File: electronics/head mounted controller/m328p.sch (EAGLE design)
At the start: 40 parts, among them J2 M02PTH, U1 ATMEGA328P, U2 V_REG_MIC2920, X1 16MHz

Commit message: pre-production PCBs
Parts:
- removed U$1, U$2: JST-PH3, jst-ph:JST-PH3
- added HEAD-DATA, HEAD-PWR: (no value), jst-ph:JST-PH2
- LIM-X, LIM-Y, LIM-Z: value JST-PH3 -> (none); device jst-ph:JST-PH3 -> jst-ph:JST-PH2
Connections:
- net 12V: now also HEAD-PWR.1; no longer U$1.1
- net GND: now also HEAD-PWR.2; no longer U$1.2
- net RX: now also HEAD-DATA.1; no longer U$2.1
- net TX: now also HEAD-DATA.2; no longer U$2.2
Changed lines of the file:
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@@
 <part name="STANDOFF3" library="SparkFun-Electromechanical" deviceset="STAND-OFF" device="TIGHT"/>
 <part name="STANDOFF4" library="SparkFun-Electromechanical" deviceset="STAND-OFF" device="TIGHT"/>
-<part name="LIM-X" library="jst-ph" deviceset="JST-PH3" device=""/>
-<part name="LIM-Y" library="jst-ph" deviceset="JST-PH3" device=""/>
-<part name="LIM-Z" library="jst-ph" deviceset="JST-PH3" device=""/>
+<part name="LIM-X" library="jst-ph" deviceset="JST-PH2" device=""/>
+<part name="LIM-Y" library="jst-ph" deviceset="JST-PH2" device=""/>
+<part name="LIM-Z" library="jst-ph" deviceset="JST-PH2" device=""/>
 <part name="DRV-Z" library="SparkFun-Connectors" deviceset="M06" device="LOCK"/>
 <part name="DRV-Y" library="SparkFun-Connectors" deviceset="M06" device="LOCK"/>
@@
 <part name="AUX-X" library="SparkFun-Connectors" deviceset="M06" device="LOCK"/>
 <part name="GND3" library="SparkFun-Aesthetics" deviceset="GND" device=""/>
-<part name="U2" library="SparkFun-PowerIC" deviceset="V_REG_MIC2920" device=""/>
 <part name="GND4" library="SparkFun-Aesthetics" deviceset="GND" device=""/>
 <part name="C12" library="adafruit" deviceset="C-US" device="C1206" value="10u"/>
@@
 <part name="C3" library="adafruit" deviceset="C-US" device="C0603" value="100n"/>
 <part name="GND5" library="SparkFun-Aesthetics" deviceset="GND" device=""/>
-<part name="U$1" library="jst-ph" deviceset="JST-PH3" device=""/>
-<part name="U$2" library="jst-ph" deviceset="JST-PH3" device=""/>
+<part name="HEAD-PWR" library="jst-ph" deviceset="JST-PH2" device=""/>
+<part name="HEAD-DATA" library="jst-ph" deviceset="JST-PH2" device=""/>
 <part name="C9" library="adafruit" deviceset="C-US" device="C1206" value="10u"/>
 <part name="C10" library="adafruit" deviceset="C-US" device="C1206" value="10u"/>
 <part name="C11" library="adafruit" deviceset="C-US" device="C1206" value="10u"/>
+<part name="U2" library="SparkFun-PowerIC" deviceset="V_REG_MIC2920" device=""/>
 </parts>
 <sheets>
@@
 <instance part="AUX-X" gate="G$1" x="195.58" y="7.62"/>
 <instance part="GND3" gate="1" x="180.34" y="25.4"/>
-<instance part="U2" gate="G$1" x="154.94" y="104.14" smashed="yes">
-<attribute name="NAME" x="157.48" y="96.52" size="1.778" layer="95"/>
-</instance>
 <instance part="GND4" gate="1" x="154.94" y="91.44"/>
 <instance part="C12" gate="G$1" x="167.64" y="101.6"/>
@@
 <instance part="C3" gate="G$1" x="20.32" y="63.5"/>
 <instance part="GND5" gate="1" x="81.28" y="86.36"/>
-<instance part="U$1" gate="G$1" x="86.36" y="96.52" smashed="yes">
-<attribute name="NAME" x="83.82" y="102.362" size="1.778" layer="95"/>
-</instance>
-<instance part="U$2" gate="G$1" x="86.36" y="111.76" smashed="yes">
-<attribute name="NAME" x="83.82" y="117.602" size="1.778" layer="95"/>
+<instance part="HEAD-PWR" gate="G$1" x="86.36" y="96.52" smashed="yes">
+<attribute name="NAME" x="83.82" y="99.822" size="1.778" layer="95"/>
+</instance>
+<instance part="HEAD-DATA" gate="G$1" x="86.36" y="111.76" smashed="yes">
+<attribute name="NAME" x="83.82" y="115.062" size="1.778" layer="95"/>
 </instance>
 <instance part="C9" gate="G$1" x="124.46" y="101.6"/>
 <instance part="C10" gate="G$1" x="132.08" y="101.6"/>
 <instance part="C11" gate="G$1" x="139.7" y="101.6"/>
+<instance part="U2" gate="G$1" x="154.94" y="104.14" smashed="yes">
+<attribute name="NAME" x="157.48" y="96.52" size="1.778" layer="95"/>
+</instance>
 </instances>
 <busses>
@@
 <wire x1="60.96" y1="96.52" x2="81.28" y2="96.52" width="0.1524" layer="91"/>
 <wire x1="81.28" y1="96.52" x2="81.28" y2="88.9" width="0.1524" layer="91"/>
-<wire x1="93.98" y1="96.52" x2="99.06" y2="96.52" width="0.1524" layer="91"/>
+<wire x1="93.98" y1="93.98" x2="99.06" y2="93.98" width="0.1524" layer="91"/>
 <wire x1="81.28" y1="88.9" x2="99.06" y2="88.9" width="0.1524" layer="91"/>
-<wire x1="99.06" y1="88.9" x2="99.06" y2="96.52" width="0.1524" layer="91"/>
+<wire x1="99.06" y1="88.9" x2="99.06" y2="93.98" width="0.1524" layer="91"/>
 <junction x="81.28" y="88.9"/>
-<pinref part="U$1" gate="G$1" pin="2"/>
+<pinref part="HEAD-PWR" gate="G$1" pin="2"/>
 </segment>
 <segment>
@@
 <wire x1="170.18" y1="58.42" x2="175.26" y2="58.42" width="0.1524" layer="91"/>
 <wire x1="175.26" y1="58.42" x2="195.58" y2="58.42" width="0.1524" layer="91"/>
-<wire x1="193.04" y1="66.04" x2="195.58" y2="66.04" width="0.1524" layer="91"/>
-<wire x1="195.58" y1="66.04" x2="195.58" y2="58.42" width="0.1524" layer="91"/>
+<wire x1="193.04" y1="63.5" x2="195.58" y2="63.5" width="0.1524" layer="91"/>
+<wire x1="195.58" y1="63.5" x2="195.58" y2="58.42" width="0.1524" layer="91"/>
 <pinref part="LIM-Y" gate="G$1" pin="2"/>
-<wire x1="167.64" y1="66.04" x2="170.18" y2="66.04" width="0.1524" layer="91"/>
-<wire x1="170.18" y1="66.04" x2="170.18" y2="58.42" width="0.1524" layer="91"/>
+<wire x1="167.64" y1="63.5" x2="170.18" y2="63.5" width="0.1524" layer="91"/>
+<wire x1="170.18" y1="63.5" x2="170.18" y2="58.42" width="0.1524" layer="91"/>
 <pinref part="LIM-X" gate="G$1" pin="2"/>
-<wire x1="142.24" y1="66.04" x2="144.78" y2="66.04" width="0.1524" layer="91"/>
-<wire x1="144.78" y1="66.04" x2="144.78" y2="58.42" width="0.1524" layer="91"/>
+<wire x1="142.24" y1="63.5" x2="144.78" y2="63.5" width="0.1524" layer="91"/>
+<wire x1="144.78" y1="63.5" x2="144.78" y2="58.42" width="0.1524" layer="91"/>
 <pinref part="C13" gate="G$1" pin="2"/>
 <wire x1="149.86" y1="60.96" x2="149.86" y2="58.42" width="0.1524" layer="91"/>
@@
 <segment>
 <pinref part="GND4" gate="1" pin="GND"/>
-<pinref part="U2" gate="G$1" pin="GND"/>
 <wire x1="154.94" y1="93.98" x2="154.94" y2="96.52" width="0.1524" layer="91"/>
 <pinref part="C8" gate="G$1" pin="2"/>
@@
 <pinref part="C11" gate="G$1" pin="2"/>
 <junction x="139.7" y="96.52"/>
+<pinref part="U2" gate="G$1" pin="GND"/>
 </segment>
 </net>
@@
 </segment>
 <segment>
-<pinref part="U$2" gate="G$1" pin="1"/>
-<wire x1="93.98" y1="114.3" x2="99.06" y2="114.3" width="0.1524" layer="91"/>
-<label x="93.98" y="114.3" size="1.778" layer="95"/>
+<pinref part="HEAD-DATA" gate="G$1" pin="1"/>
+<wire x1="93.98" y1="111.76" x2="99.06" y2="111.76" width="0.1524" layer="91"/>
+<label x="93.98" y="111.76" size="1.778" layer="95"/>
 </segment>
 </net>
@@
 </segment>
 <segment>
-<pinref part="U$2" gate="G$1" pin="2"/>
-<wire x1="93.98" y1="111.76" x2="99.06" y2="111.76" width="0.1524" layer="91"/>
-<label x="93.98" y="111.76" size="1.778" layer="95"/>
+<pinref part="HEAD-DATA" gate="G$1" pin="2"/>
+<wire x1="93.98" y1="109.22" x2="99.06" y2="109.22" width="0.1524" layer="91"/>
+<label x="93.98" y="109.22" size="1.778" layer="95"/>
 </segment>
 </net>
@@
 </segment>
 <segment>
+<wire x1="142.24" y1="66.04" x2="142.24" y2="68.58" width="0.1524" layer="91"/>
 <wire x1="142.24" y1="68.58" x2="149.86" y2="68.58" width="0.1524" layer="91"/>
 <label x="142.24" y="68.58" size="1.778" layer="95"/>
@@
 </segment>
 <segment>
+<wire x1="167.64" y1="66.04" x2="167.64" y2="68.58" width="0.1524" layer="91"/>
 <wire x1="167.64" y1="68.58" x2="175.26" y2="68.58" width="0.1524" layer="91"/>
 <label x="167.64" y="68.58" size="1.778" layer="95"/>
@@
 </segment>
 <segment>
+<wire x1="193.04" y1="66.04" x2="193.04" y2="68.58" width="0.1524" layer="91"/>
 <wire x1="193.04" y1="68.58" x2="200.66" y2="68.58" width="0.1524" layer="91"/>
 <label x="193.04" y="68.58" size="1.778" layer="95"/>
@@
 </segment>
 <segment>
-<pinref part="U2" gate="G$1" pin="OUT"/>
 <wire x1="162.56" y1="104.14" x2="167.64" y2="104.14" width="0.1524" layer="91"/>
 <label x="160.02" y="104.14" size="1.778" layer="95"/>
 <pinref part="C12" gate="G$1" pin="1"/>
+<pinref part="U2" gate="G$1" pin="OUT"/>
 </segment>
 <segment>
@@
 <net name="12V" class="0">
 <segment>
-<label x="93.98" y="99.06" size="1.778" layer="95"/>
-<wire x1="93.98" y1="99.06" x2="104.14" y2="99.06" width="0.1524" layer="91"/>
-<wire x1="104.14" y1="99.06" x2="104.14" y2="104.14" width="0.1524" layer="91"/>
-<pinref part="U2" gate="G$1" pin="IN"/>
+<label x="96.52" y="96.52" size="1.778" layer="95"/>
+<wire x1="93.98" y1="96.52" x2="104.14" y2="96.52" width="0.1524" layer="91"/>
+<wire x1="104.14" y1="96.52" x2="104.14" y2="104.14" width="0.1524" layer="91"/>
 <wire x1="104.14" y1="104.14" x2="109.22" y2="104.14" width="0.1524" layer="91"/>
 <pinref part="C8" gate="G$1" pin="1"/>
@@
 <pinref part="R1" gate="G$1" pin="2"/>
 <junction x="109.22" y="104.14"/>
-<pinref part="U$1" gate="G$1" pin="1"/>
+<pinref part="HEAD-PWR" gate="G$1" pin="1"/>
 <pinref part="C9" gate="G$1" pin="1"/>
 <wire x1="124.46" y1="104.14" x2="132.08" y2="104.14" width="0.1524" layer="91"/>
@@
 <wire x1="139.7" y1="104.14" x2="147.32" y2="104.14" width="0.1524" layer="91"/>
 <junction x="139.7" y="104.14"/>
-</segment>
-<segment>
+<pinref part="U2" gate="G$1" pin="IN"/>
+</segment>
+<segment>

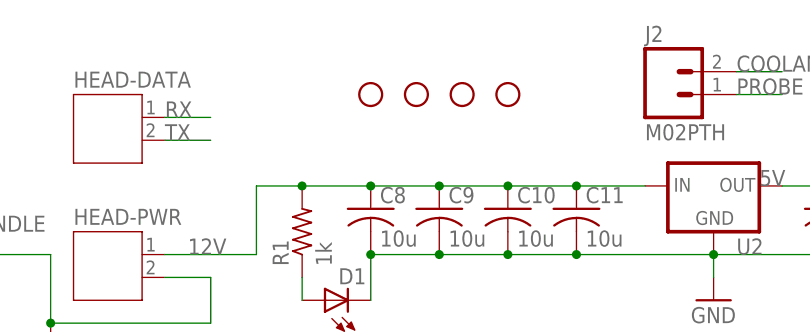
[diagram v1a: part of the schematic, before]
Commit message: updated all PCBs and added PDF schematics
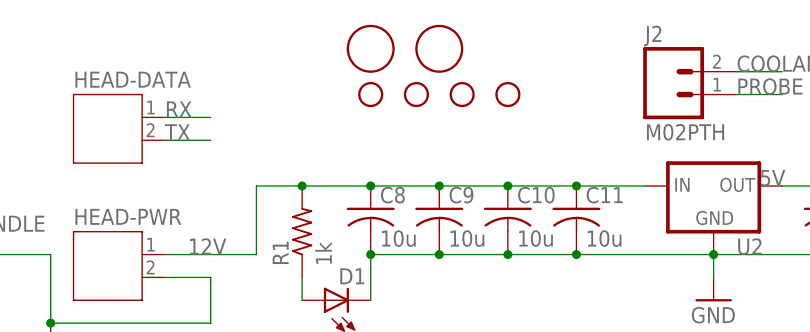
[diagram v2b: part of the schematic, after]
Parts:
- added U$1, U$2: FIDUCIAL, adafruit:FIDUCIAL
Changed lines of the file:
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@@
 <part name="C11" library="adafruit" deviceset="C-US" device="C1206" value="10u"/>
 <part name="U2" library="SparkFun-PowerIC" deviceset="V_REG_MIC2920" device=""/>
+<part name="U$1" library="adafruit" deviceset="FIDUCIAL" device=""/>
+<part name="U$2" library="adafruit" deviceset="FIDUCIAL" device=""/>
 </parts>
 <sheets>
@@
 <attribute name="NAME" x="157.48" y="96.52" size="1.778" layer="95"/>
 </instance>
+<instance part="U$1" gate="G$1" x="116.84" y="119.38"/>
+<instance part="U$2" gate="G$1" x="124.46" y="119.38"/>
 </instances>
 <busses>
